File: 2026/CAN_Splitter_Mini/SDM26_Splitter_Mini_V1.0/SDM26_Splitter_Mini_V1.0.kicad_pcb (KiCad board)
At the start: 2 copper layers, 16.2 x 32 mm, 7 parts, among them J1 Conn_01x04_Socket, J2 Conn_01x04_Socket, J3 Conn_01x04_Socket

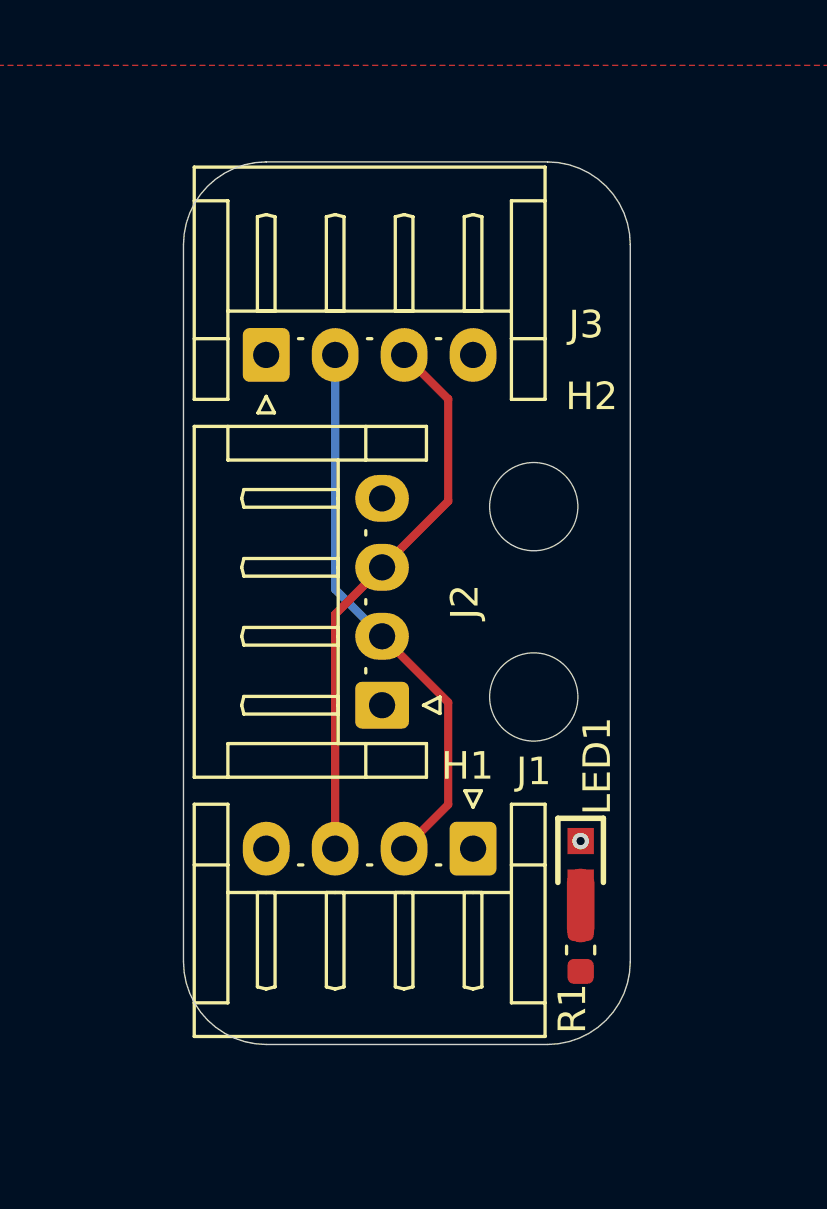
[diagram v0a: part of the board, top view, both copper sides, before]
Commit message: Moved Mini edge connectors
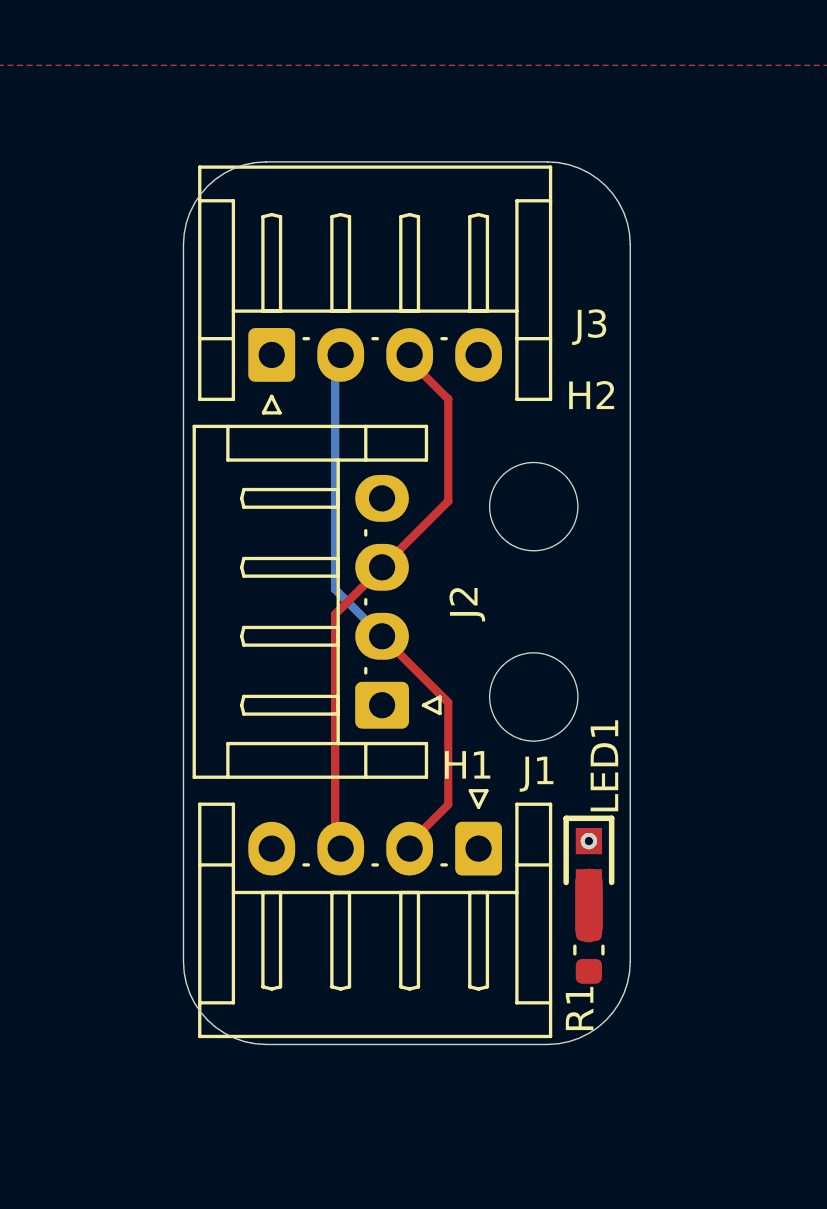
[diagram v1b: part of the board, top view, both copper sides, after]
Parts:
- moved LED1 0.30 mm to (111.2, 96.9)
- moved R1 0.30 mm to (111.2, 100.1)
- moved J1 0.20 mm to (107.2, 96.4)
- moved J3 0.20 mm to (99.7, 78.5)
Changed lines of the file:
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@@
 	(footprint "Connector_JST:JST_EH_S4B-EH_1x04_P2.50mm_Horizontal"
 		(layer "F.Cu")
-		(at 107 96.4 180)
+		(at 107.2 96.4 180)
 		(descr "JST EH series connector, S4B-EH (http://www.jst-mfg.com/product/pdf/eng/eEH.pdf), generated with kicad-footprint-generator")
 		(tags "connector JST EH horizontal")
@@
 	(footprint "Capacitor_SMD:C_0603_1608Metric"
 		(layer "F.Cu")
-		(at 110.9 100.075 -90)
+		(at 111.2 100.075 -90)
 		(descr "Capacitor SMD 0603 (1608 Metric), square (rectangular) end terminal, IPC-7351 nominal, (Body size source: IPC-SM-782 page 76, https://www.pcb-3d.com/wordpress/wp-content/uploads/ipc-sm-782a_amendment_1_and_2.pdf), generated with kicad-footprint-generator")
 		(tags "capacitor")
@@
 	(footprint "SDM_MiscFootprint:LEDC1608X80N"
 		(layer "F.Cu")
-		(at 110.9 96.875 -90)
+		(at 111.2 96.875 -90)
 		(descr "WL-SMCW")
 		(tags "LED")
@@
 	(footprint "Connector_JST:JST_EH_S4B-EH_1x04_P2.50mm_Horizontal"
 		(layer "F.Cu")
-		(at 99.5 78.5)
+		(at 99.7 78.5)
 		(descr "JST EH series connector, S4B-EH (http://www.jst-mfg.com/product/pdf/eng/eEH.pdf), generated with kicad-footprint-generator")
 		(tags "connector JST EH horizontal")
@@
 	)
 	(via
-		(at 110.9 96.125)
+		(at 111.2 96.125)
 		(size 0.6)
 		(drill 0.3)
@@
 	)
 	(segment
-		(start 110.9 99.3)
-		(end 110.9 97.625)
+		(start 111.2 99.3)
+		(end 111.2 97.625)
 		(width 1)
 		(layer "F.Cu")
